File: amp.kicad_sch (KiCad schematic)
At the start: 32 parts, among them J10 JST_SH_1x4_SM04B-SRSS-TB-LF-SN, J12 JST_SH_1x2_SM02B-SRSS-TB-LF-SN, J5 Phone_TRS_MiniJack_SJ-3523-SM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, J9 JST_SUR_1x5_BM05B-SURS-TB-LF-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, U3 TAS2505IRGER, Y2 Oscillator_50MHz_ECS_1612MV

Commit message: [#71986] Replace AMP with MAX98357AA
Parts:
- removed C18, C20: C_10u_10V_0402, antmicro-footprints:C_0402_1005Metric, symbol antmicroCapacitors0402:C_10u_10V_0402
- removed C19, C21, C23, C24, C27: C_100n_0402, antmicro-footprints:C_0402_1005Metric, symbol antmicroCapacitors0402:C_100n_0402
- removed C22, C25: C_22u_25V_0805, antmicro-footprints:C_0805_2012Metric, symbol antmicroCapacitorsmisc:C_22u_25V_0805
- removed C26: C_47u_0603, antmicro-footprints:C_0603_1608Metric, symbol antmicroCapacitors0603:C_47u_0603
- removed J5: Phone_TRS_MiniJack_SJ-3523-SMT-TR, antmicro-footprints:Phone_TRS_MiniJack_SJ-3523-SMT-TR, symbol antmicroBarrelAudioConnectors:Phone_TRS_MiniJack_SJ-3523-SMT-TR
- removed R11, R12: R_2k7_0402, antmicro-footprints:R_0402_1005Metric, symbol antmicroResistors0402:R_2k7_0402
- removed R17: R_10k_0402, antmicro-footprints:R_0402_1005Metric, symbol antmicroResistors0402:R_10k_0402
- removed R26, R27, R35: R_0R_0402, antmicro-footprints:R_0402_1005Metric, symbol antmicroResistors0402:R_0R_0402
- removed U3: TAS2505IRGER, antmicro-footprints:QFN-24-1EP_4x4mm_P0.5mm_EP2.7x2.7mm, symbol antmicroInterfaceControllers:TAS2505IRGER
- removed Y2: Oscillator_50MHz_ECS_1612MV, antmicro-footprints:Oscillator_SMD_ECS_1612MV_1.6x1.2x0.6mm, symbol antmicroOscillators:Oscillator_50MHz_ECS_1612MV
- added C26, C62, C65, C67, C68: C_100n_0402, antmicro-footprints:C_0402_1005Metric, symbol antmicroCapacitors0402:C_100n_0402
- added C63, C69: C_22u_25V_0805, antmicro-footprints:C_0805_2012Metric, symbol antmicroCapacitorsmisc:C_22u_25V_0805
- added C64, C66: C_10u_10V_0402, antmicro-footprints:C_0402_1005Metric, symbol antmicroCapacitors0402:C_10u_10V_0402
- added R100, R35: R_100k_0402, antmicro-footprints:R_0402_1005Metric, symbol antmicroResistors0402:R_100k_0402
- added R11, R12, R17, R71, R72, R96, R97, R98, R99: R_0R_0402, antmicro-footprints:R_0402_1005Metric, symbol antmicroResistors0402:R_0R_0402
- added R26: R_1k_0402, antmicro-footprints:R_0402_1005Metric, symbol antmicroResistors0402:R_1k_0402
- added R27: R_390R_0402, antmicro-footprints:R_0402_1005Metric, symbol antmicroResistors0402:R_390R_0402
- added R63: R_10k_0402, antmicro-footprints:R_0402_1005Metric, symbol antmicroResistors0402:R_10k_0402
- added R73, R95: R_2k7_0402, antmicro-footprints:R_0402_1005Metric, symbol antmicroResistors0402:R_2k7_0402
- added U17: MAX98357A, antmicro-footprints:TQFN-16-1EP_3x3mm_P0.5mm, symbol antmicroInterfaceControllers:MAX98357A
- added U18: TAS2505IRGER, antmicro-footprints:QFN-24-1EP_4x4mm_P0.5mm_EP2.7x2.7mm, symbol antmicroInterfaceControllers:TAS2505IRGER
- added Y4: Oscillator_50MHz_ECS_1612MV, antmicro-footprints:Oscillator_SMD_ECS_1612MV_1.6x1.2x0.6mm, symbol antmicroOscillators:Oscillator_50MHz_ECS_1612MV
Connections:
- net +1V8: now also C26.2, C66.2, C67.2, C68.2, C69.2, U18.23 (DVDD), U18.7 (AVDD), Y4.1 (EN), Y4.4 (VDD)
- net +3V3: now also C64.2, C65.2, R11.2, R63.1, R71.2, R73.2, R95.2, U18.22 (IOVDD)
- net +5V: now also R16.2, R100.2, R12.2, R26.2, R27.2, R72.2, R99.2; no longer R36.2
- net 50M_CLK: now also U18.16 (MCLK), Y4.3 (OUT)
- net AMP_NRST: now also R63.2, U18.2 (~{RST})
- net GND: now also R36.1, C26.1, C62.1, C63.1, C64.1, C65.1, C66.1, C67.1, C68.1, C69.1, R17.1, R35.1, U17.11 (GND), U17.15 (GND), U17.17 (EP), U17.3 (GND), U18.1 (SPI_SEL), U18.11 (SPKVSS), U18.21 (SCLK), U18.24 (DVSS), U18.25 (EP), U18.6 (AVSS), U18.8 (LDO_SEL), Y4.2 (GND)
- net HPOUT: now also U18.5 (HPOUT)
- net I2C.SCL: now also R95.1, R96.1
- net I2C.SDA: now also R73.1, R97.2
- net I2S.SCK: now also U17.16 (BCLK), U18.15 (BCLK)
- net I2S.SD: now also U17.1 (DIN), U18.13 (DIN)
- net I2S.WS: now also U17.14 (LRCLK), U18.14 (WCLK)
- net SPKVDD: now also C62.2, C63.2, R71.1, R72.1, U18.10 (SPKVDD); no longer R36.1
- net SPK_M: now also U17.10 (OUT_N), U18.9 (SPKM)
- net SPK_P: now also U17.9 (OUT_P), U18.12 (SPKP)
- net ~{SD_MODE}: now reaches R16.1
- net ~{SD_MODE}: now also R17.2, R26.1, R27.1, U17.4 (~{SD_MODE})
- new net: U17.12 (NC), U17.13 (NC), U17.5 (NC), U17.6 (NC)
- new net: R96.2, U18.19 (SCL)
- new net: R97.1, U18.20 (SDA)
- new net: R98.1, U18.3 (AINL)
- new net: R98.2, U18.4 (AINR)
- new net GAIN: R100.1, R35.2, R36.2, R99.1, U17.2 (GAIN_SLOT)
- new net VDD: R11.1, R12.1, U17.7 (VDD), U17.8 (VDD)
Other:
- note added: "12 dB"
- note added: "15 dB"
- note added: "3 dB"
- note added: "6 dB"
- note added: "9 dB"
- note added: "Unconnected"
- note added: "datasheet pg.17"
- note added: "datasheet pg.28"
- note removed: "Headphones 3.5mm Jack"

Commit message: [#71986] Finish sch  MAX98357AA
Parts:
- removed C26, C62, C65, C67, C68: C_100n_0402, antmicro-footprints:C_0402_1005Metric, symbol antmicroCapacitors0402:C_100n_0402
- removed C63, C69: C_22u_25V_0805, antmicro-footprints:C_0805_2012Metric, symbol antmicroCapacitorsmisc:C_22u_25V_0805
- removed C64, C66: C_10u_10V_0402, antmicro-footprints:C_0402_1005Metric, symbol antmicroCapacitors0402:C_10u_10V_0402
- removed D8, D9: TPD1E0B04_XDFN-2, antmicro-footprints:XDFN-2_1x0.60mm, symbol antmicroTVSDiodes:TPD1E0B04_XDFN-2
- removed J10: JST_SH_1x4_SM04B-SRSS-TB-LF-SN, antmicro-footprints:Conn_JST_SH_1x4_SM04B-SRSS-TB-LF-SN, symbol antmicroWire2BoardConnectors:JST_SH_1x4_SM04B-SRSS-TB-LF-SN
- removed R11, R12, R71, R72, R96, R97, R98: R_0R_0402, antmicro-footprints:R_0402_1005Metric, symbol antmicroResistors0402:R_0R_0402
- removed R26: R_1k_0402, antmicro-footprints:R_0402_1005Metric, symbol antmicroResistors0402:R_1k_0402
- removed R27: R_390R_0402, antmicro-footprints:R_0402_1005Metric, symbol antmicroResistors0402:R_390R_0402
- removed R63: R_10k_0402, antmicro-footprints:R_0402_1005Metric, symbol antmicroResistors0402:R_10k_0402
- removed R73, R95: R_2k7_0402, antmicro-footprints:R_0402_1005Metric, symbol antmicroResistors0402:R_2k7_0402
- removed U18: TAS2505IRGER, antmicro-footprints:QFN-24-1EP_4x4mm_P0.5mm_EP2.7x2.7mm, symbol antmicroInterfaceControllers:TAS2505IRGER
- removed Y4: Oscillator_50MHz_ECS_1612MV, antmicro-footprints:Oscillator_SMD_ECS_1612MV_1.6x1.2x0.6mm, symbol antmicroOscillators:Oscillator_50MHz_ECS_1612MV
- added C18: C_100n_0402, antmicro-footprints:C_0402_1005Metric, symbol antmicroCapacitors0402:C_100n_0402
- added C19: C_10u_10V_0402, antmicro-footprints:C_0402_1005Metric, symbol antmicroCapacitors0402:C_10u_10V_0402
- added R101: R_390k_0402, antmicro-footprints:R_0402_1005Metric, symbol antmicroResistors0402:R_390k_0402
- added R27: R_1M_0402, antmicro-footprints:R_0402_1005Metric, symbol antmicroResistors0402:R_1M_0402
- R100, R16, R17, R35, R36, R99: now not fitted
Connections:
- net VDD is gone; now on net +5V: U17.7 (VDD), U17.8 (VDD)
- net +5V: now also C18.2, C19.2, R101.2, R27.2
- net GND: now also C18.1, C19.1
- net ~{SD_MODE}: now also R101.1, R27.1
- no-connect marks 2 -> 0
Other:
- note added: "(Left/2 + Right/2)"
- note added: "3.2W (4Ω at 5V) 1.8W (8Ω at 5V)"
- note added: "Left Channel"
- note added: "RLARGE (kΩ) = 222.2 x 5 - 100 = 1011kΩ RSMALL (kΩ) = 94.0 x 5 - 100 = 370kΩ"
- note added: "Right Channel"
- note added: "Rlarge"
- note added: "Rsmall"
- note added: "Selectable Audio Input Channel"
- note added: "Selectable Audio Output Gain"
- note added: "Shutdown"
- note removed: "2.6 W (4Ω, 5.5 V) 1.7 W (8 Ω, 5.5 V)"
- note removed: "Debug I2C Connector"
- note removed: "I2C Addr: 0x18"
- note removed: "SPKVDD has to be > than AVDD"
- note removed: "Short AIN if not used."
- moved on the sheet: C53, D10, D11, D12, J12, J9, R89, R90, U17

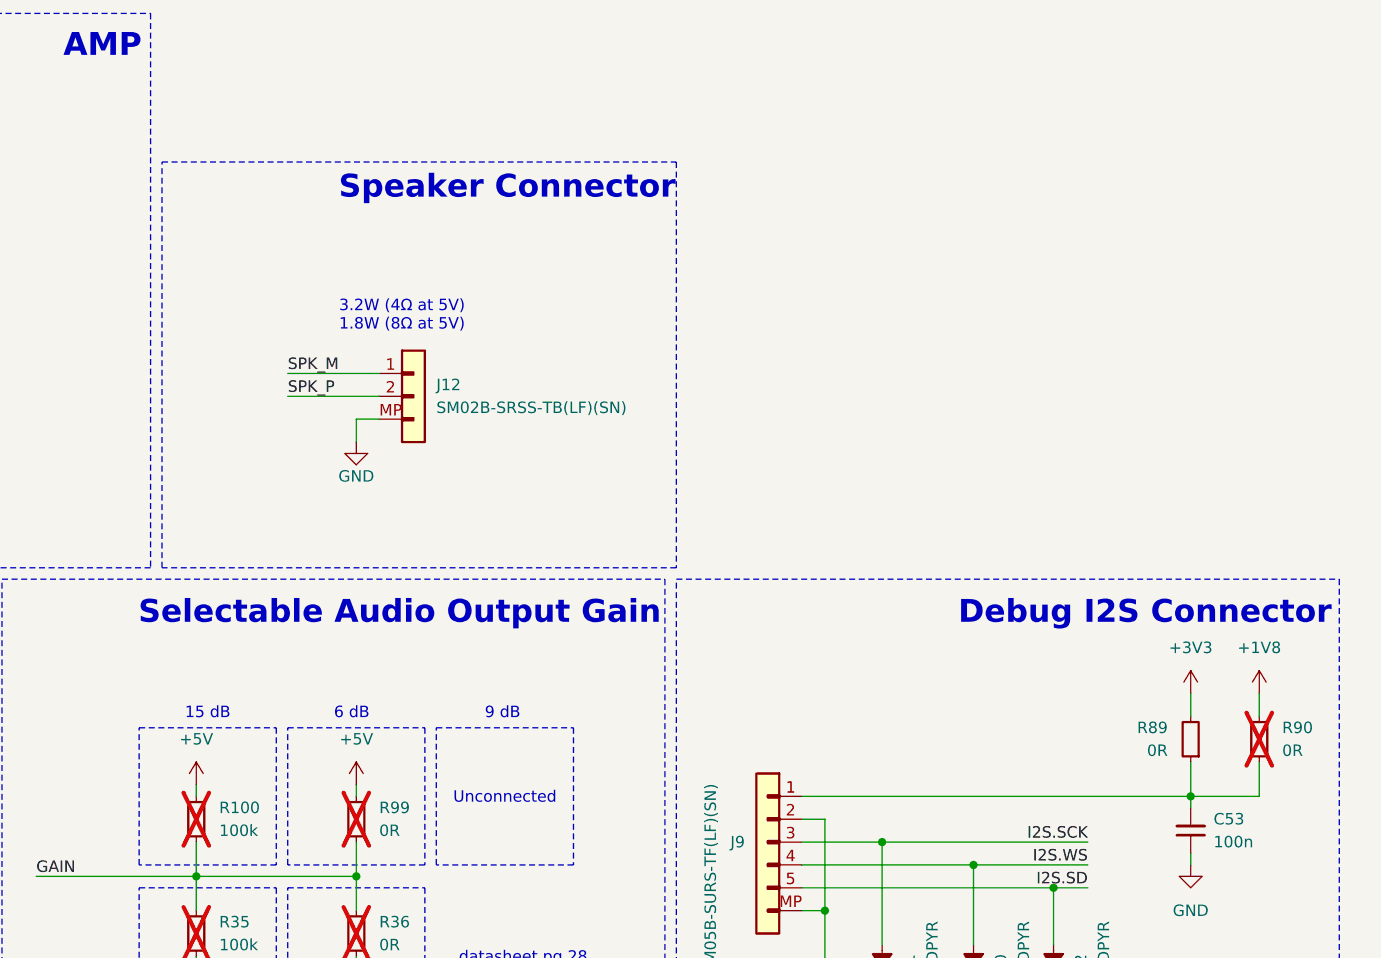
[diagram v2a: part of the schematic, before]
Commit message: [#71986] Remove 1V8 circuits after changing the AMP
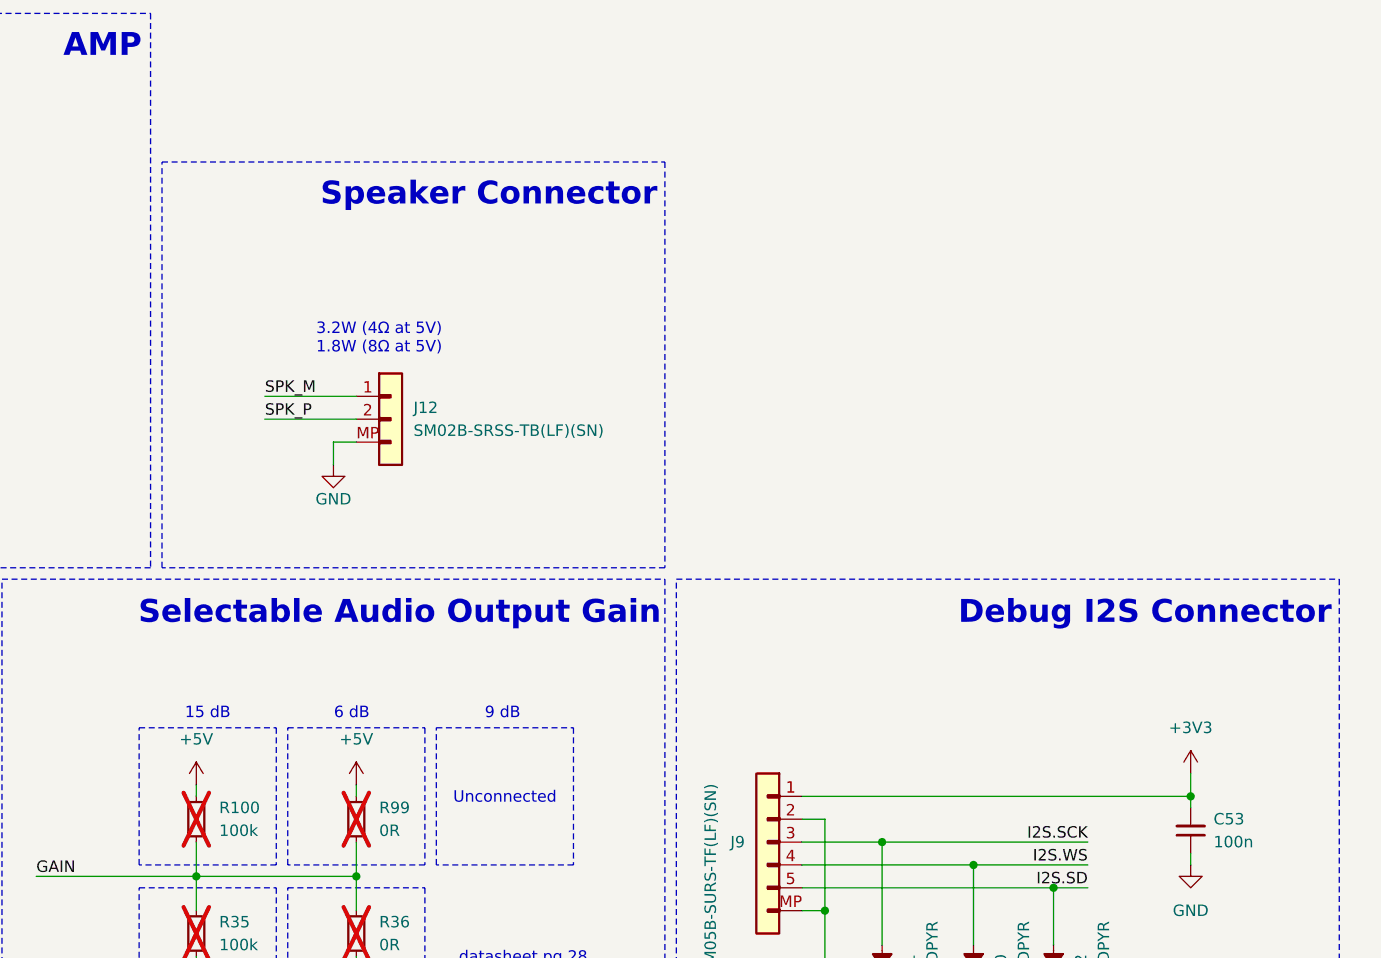
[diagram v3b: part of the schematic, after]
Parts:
- removed R89, R90: R_0R_0402, antmicro-footprints:R_0402_1005Metric, symbol antmicroResistors0402:R_0R_0402
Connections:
- net +3V3: now also C53.2, J9.1
- now unconnected: U17.12 (NC), U17.13 (NC), U17.5 (NC), U17.6 (NC)
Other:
- moved on the sheet: J12

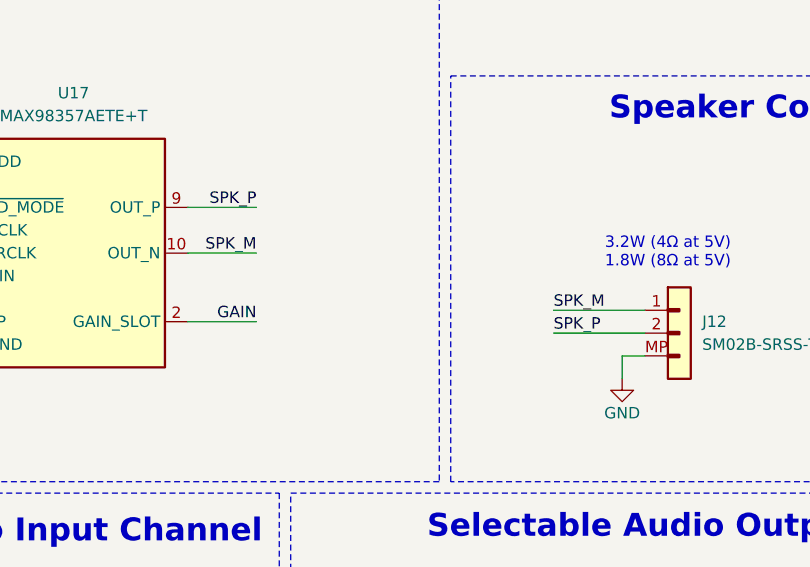
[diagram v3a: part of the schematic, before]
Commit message: [#71986] Explode subschematics
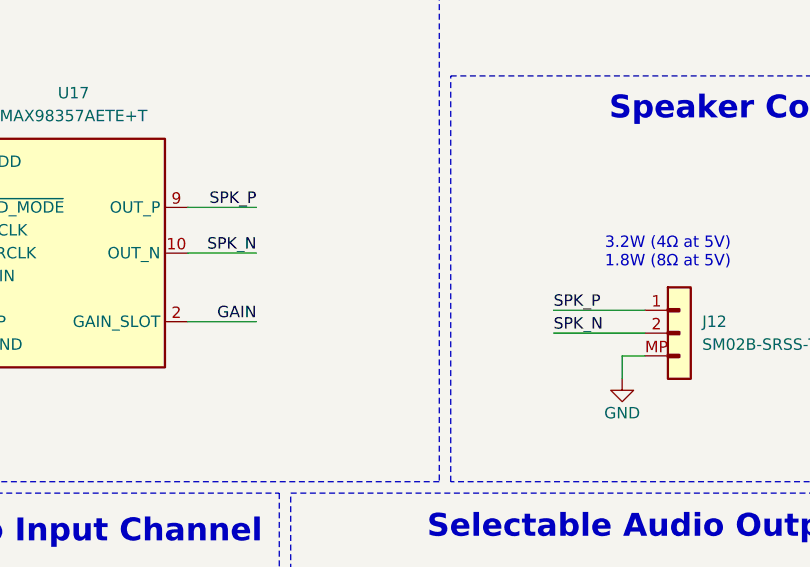
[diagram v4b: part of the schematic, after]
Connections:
- net SPK_P: now also J12.1; no longer J12.2
- net SPK_M renamed SPK_N
- net SPK_N: now also J12.2; no longer J12.1

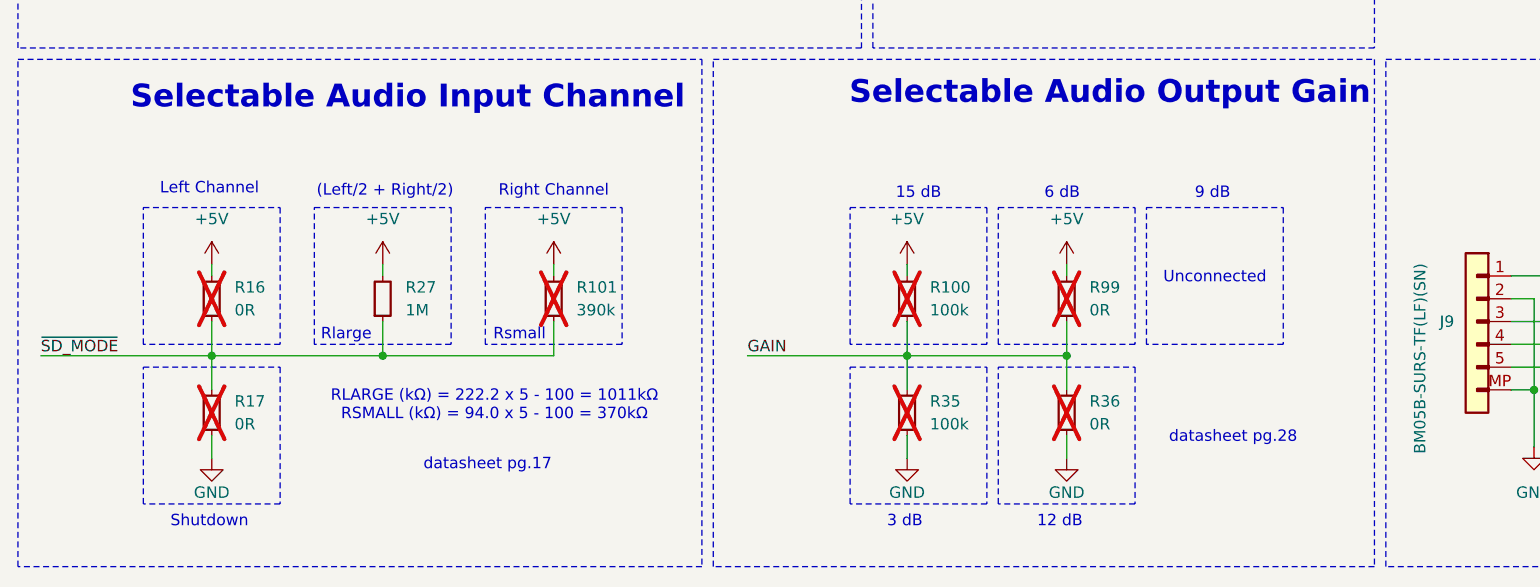
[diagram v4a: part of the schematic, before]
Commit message: [#71986] Place all components on board area
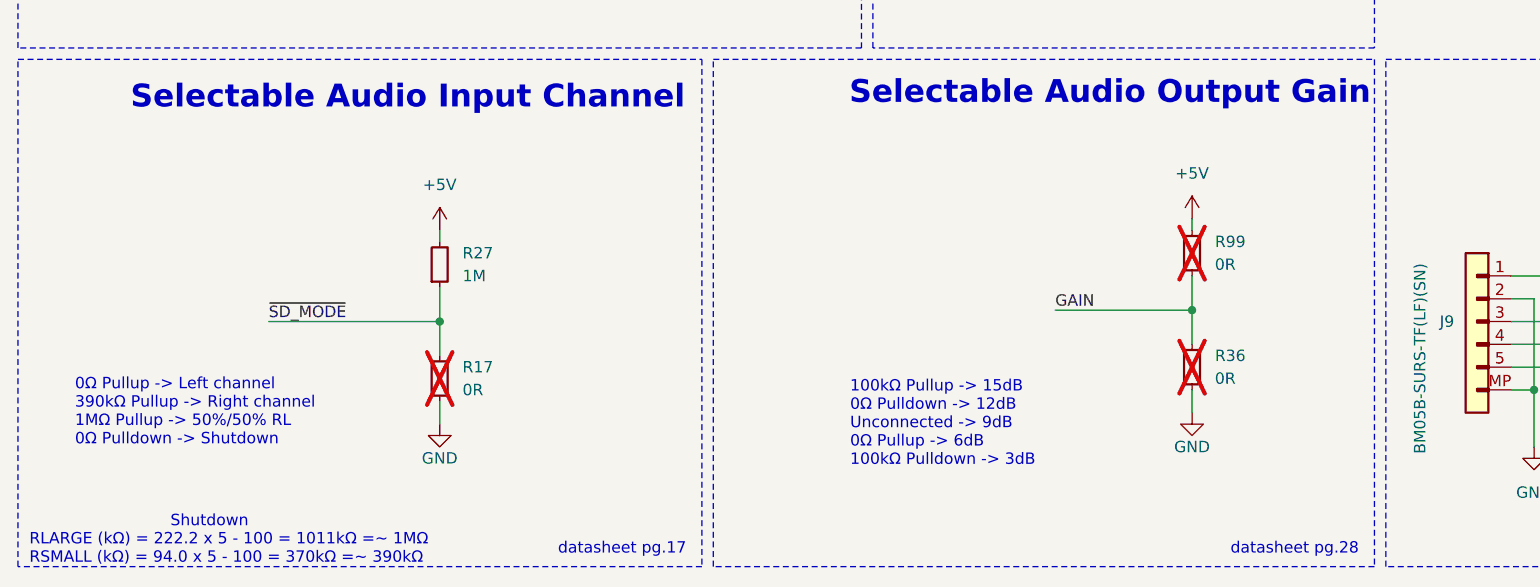
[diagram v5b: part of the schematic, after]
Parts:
- removed R100, R35: R_100k_0402, antmicro-footprints:R_0402_1005Metric, symbol antmicroResistors0402:R_100k_0402
- removed R101: R_390k_0402, antmicro-footprints:R_0402_1005Metric, symbol antmicroResistors0402:R_390k_0402
- removed R16: R_0R_0402, antmicro-footprints:R_0402_1005Metric, symbol antmicroResistors0402:R_0R_0402
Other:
- note added: "0Ω Pullup -> Left channel 390kΩ Pullup -> Right channel 1MΩ Pullup -> 50%/50% RL 0Ω Pulldown -> Shutdown"
- note added: "100kΩ Pullup -> 15dB 0Ω Pulldown -> 12dB Unconnected -> 9dB 0Ω Pullup -> 6dB 100kΩ Pulldown -> 3dB"
- note added: "RLARGE (kΩ) = 222.2 x 5 - 100 = 1011kΩ =~ 1MΩ RSMALL (kΩ) = 94.0 x 5 - 100 = 370kΩ =~ 390kΩ"
- note removed: "(Left/2 + Right/2)"
- note removed: "12 dB"
- note removed: "15 dB"
- note removed: "3 dB"
- note removed: "6 dB"
- note removed: "9 dB"
- note removed: "Left Channel"
- note removed: "RLARGE (kΩ) = 222.2 x 5 - 100 = 1011kΩ RSMALL (kΩ) = 94.0 x 5 - 100 = 370kΩ"
- note removed: "Right Channel"
- note removed: "Rlarge"
- note removed: "Rsmall"
- note removed: "Unconnected"
- moved on the sheet: R17, R27, R36, R99
